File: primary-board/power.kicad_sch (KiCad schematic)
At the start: 19 parts, among them J6 Conn_01x02, J7 Conn_01x02, J8 Conn_01x02, U2 L7806, U3 L7806, U4 AZ1117-3.3

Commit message: reorganized file tree swapped pushbuttons to smd
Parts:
- MOSFET1, MOSFET2: footprint SOT-23F_TOS -> ssm3j3:SOT-23F_TOS
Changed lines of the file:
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@@
 			)
 		)
-		(property "Footprint" "SOT-23F_TOS"
+		(property "Footprint" "ssm3j3:SOT-23F_TOS"
 			(at 232.41 74.93 0)
 			(effects
@@
 			)
 		)
-		(property "Footprint" "SOT-23F_TOS"
+		(property "Footprint" "ssm3j3:SOT-23F_TOS"
 			(at 31.75 81.28 0)
 			(effects

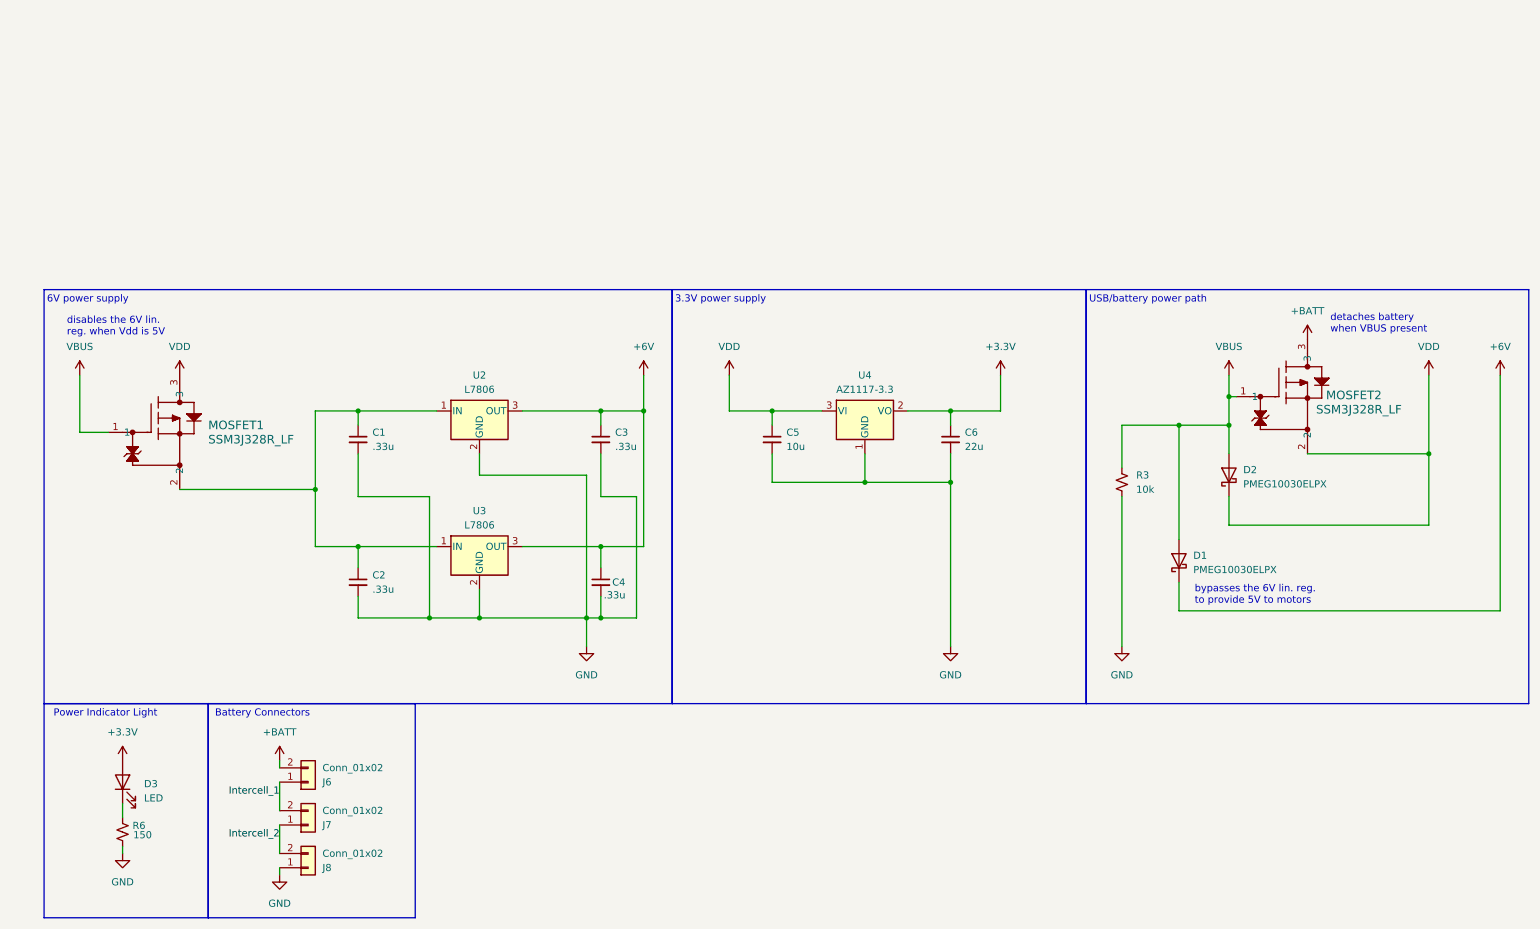
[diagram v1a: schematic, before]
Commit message: scrapped flawed power path, using a switch instead
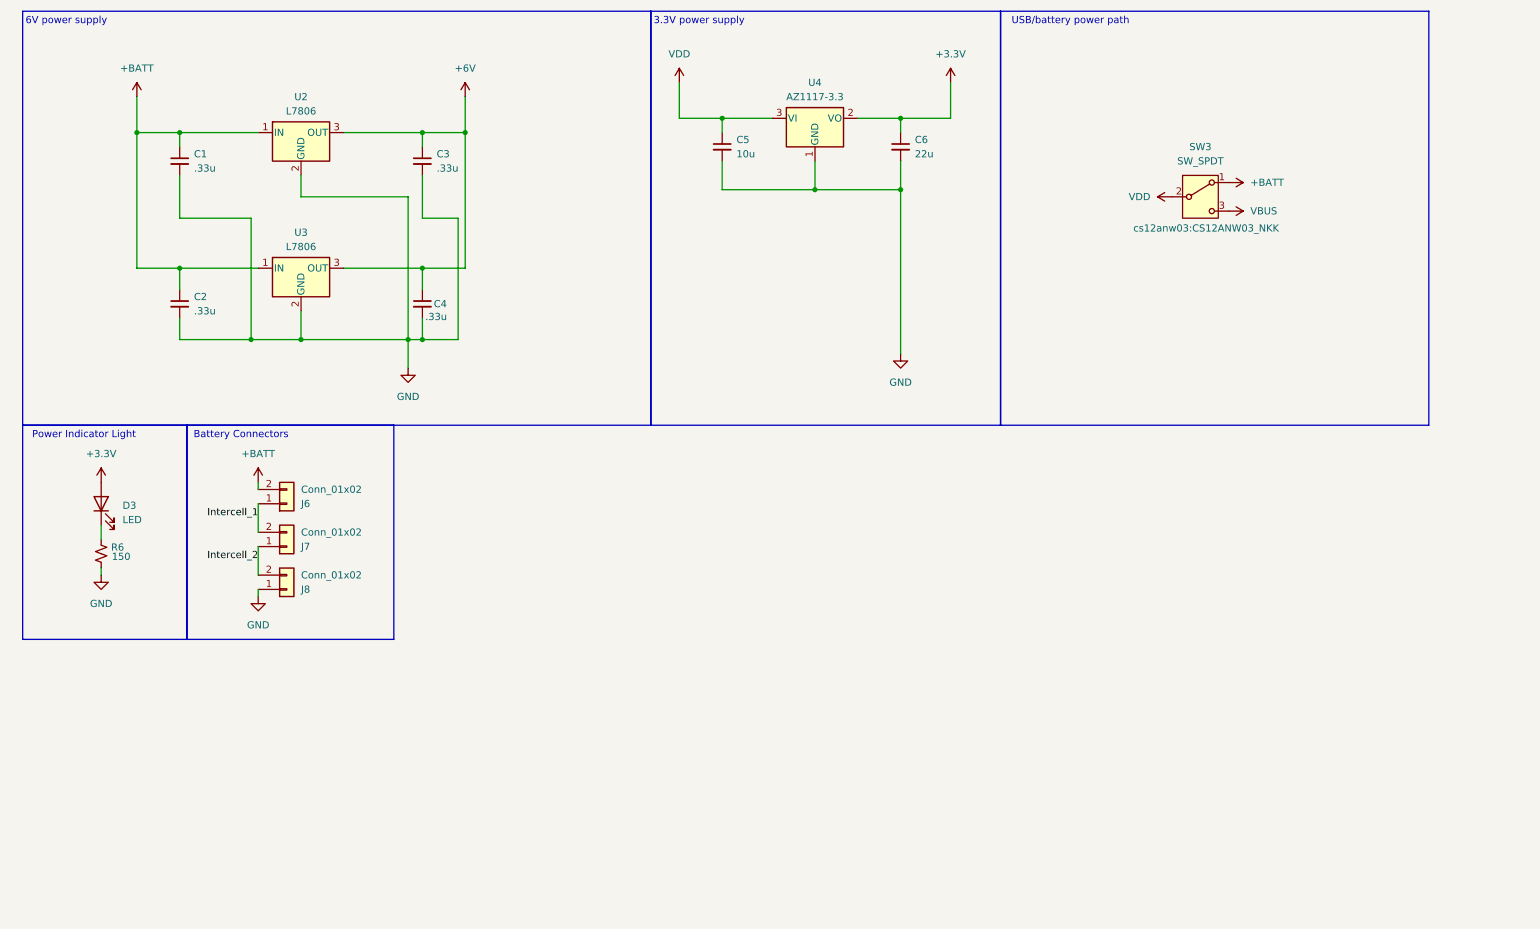
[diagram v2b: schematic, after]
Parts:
- removed D1, D2: PMEG10030ELPX, Diode_SMD:D_SOD-128, symbol Device:D_Schottky
- removed MOSFET1, MOSFET2: SSM3J328R_LF, ssm3j3:SOT-23F_TOS, symbol ssm3j3:SSM3J328R_LF
- removed R3: 10k, Resistor_SMD:R_0603_1608Metric, symbol Device:R_Small_US
- added SW3: SW_SPDT, cs12anw03:CS12ANW03_NKK, symbol Switch:SW_SPDT
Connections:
- net +BATT: now also C1.1, C2.1, U2.1 (IN), U3.1 (IN), SW3.1 (A)
- net VBUS: now also SW3.3 (C)
- net VDD: now also SW3.2 (B)
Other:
- note removed: "bypasses the 6V lin. reg. to provide 5V to motors"
- note removed: "detaches battery when VBUS present"
- note removed: "disables the 6V lin. reg. when Vdd is 5V"
- moved on the sheet: C1, C2, C3, C4, C5, C6, D3, J6, J7, J8, R6, U2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
